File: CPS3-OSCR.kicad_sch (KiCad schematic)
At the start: 17 parts, among them J1 128MB, J2 64MB, J3 CART SLOT TOP ROW, J4 CART SLOT BOTTOM ROW, J5 5145154-1, J6 Conn_02x03_Counter_Clockwise, J7 Conn_02x03_Counter_Clockwise, U1 74LS245, U2 74LS245, U3 74LS245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

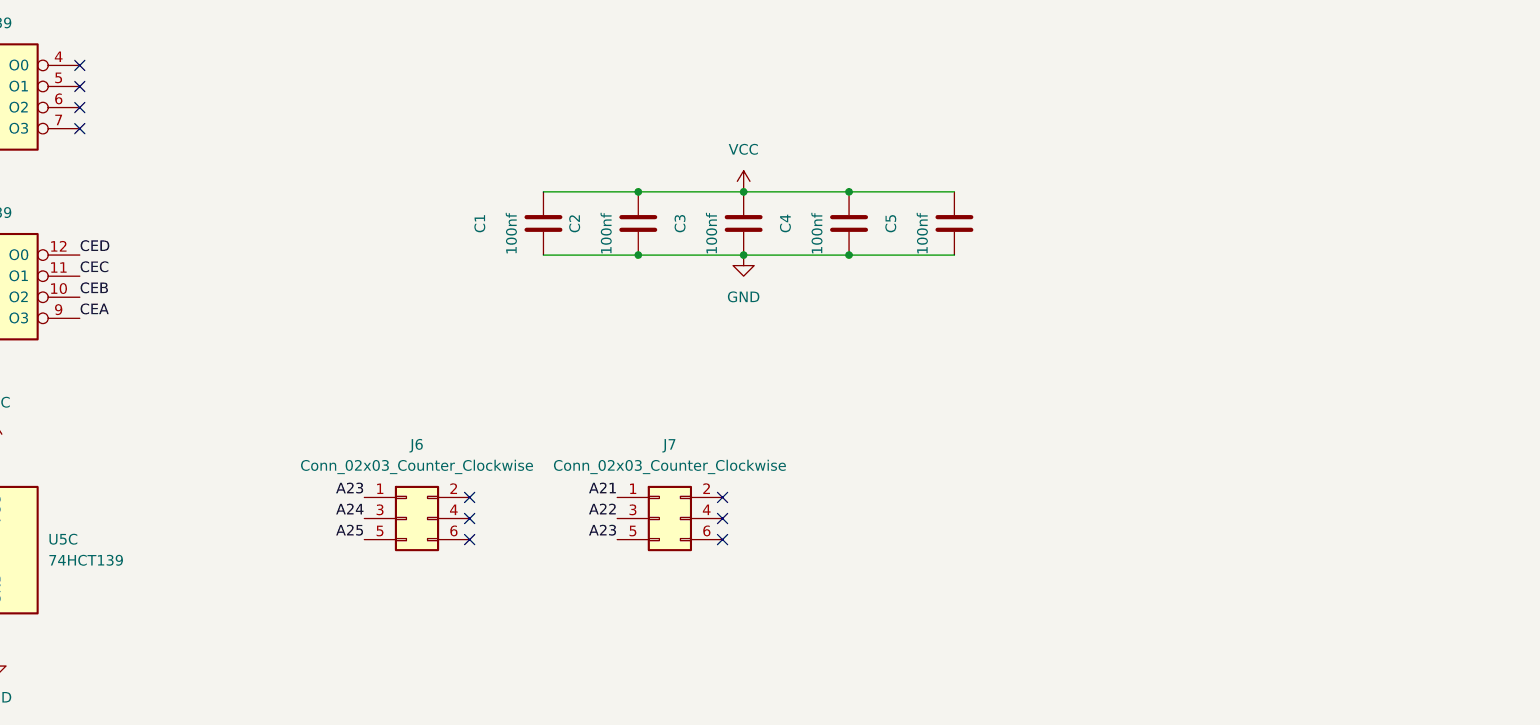
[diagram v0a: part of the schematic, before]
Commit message: Add voltage divider resitor to 3.3V and pullup's disable ic's as default
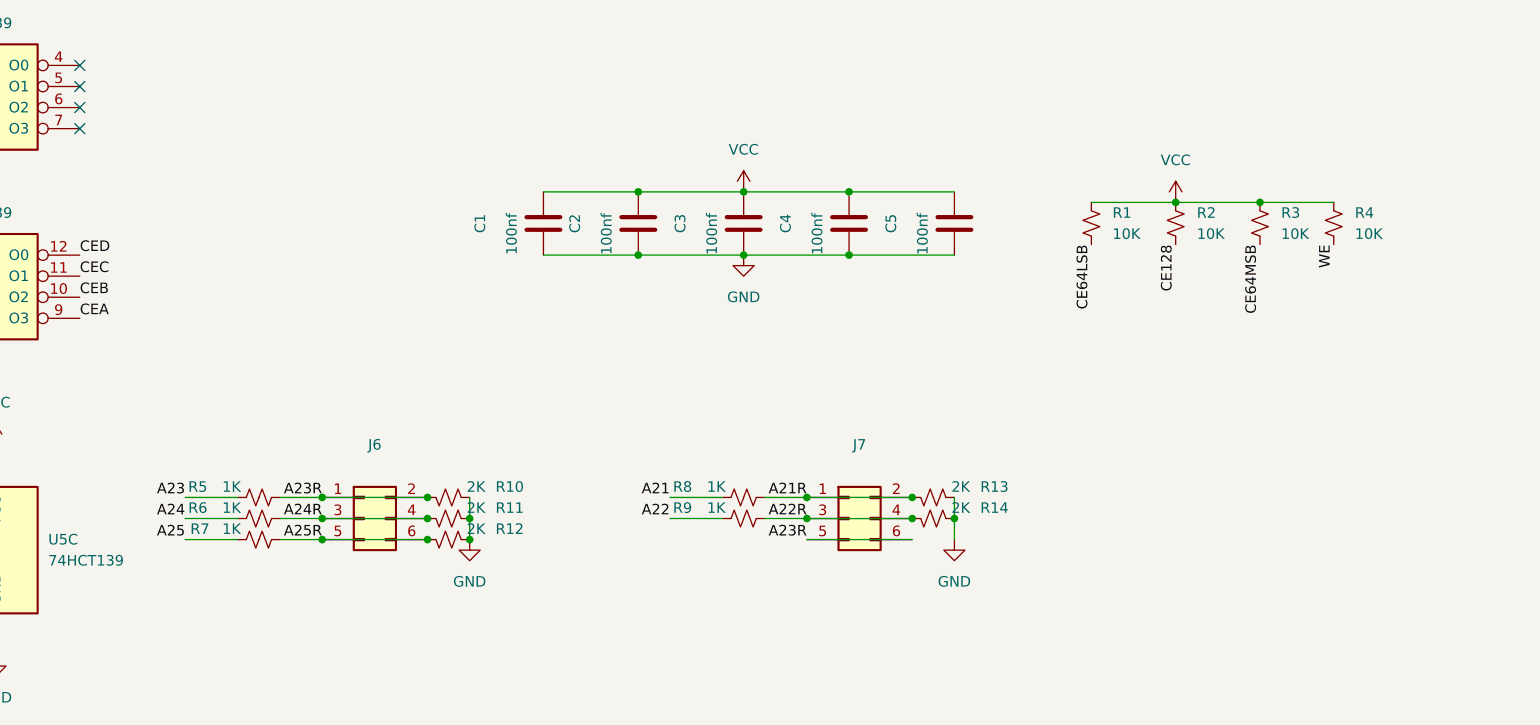
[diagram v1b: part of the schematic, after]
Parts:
- added R1, R2, R3, R4: 10K, Resistor_SMD:R_0805_2012Metric, symbol Device:R_Small_US
- added R10, R11, R12, R13, R14: 2K, Resistor_SMD:R_0805_2012Metric, symbol Device:R_Small_US
- added R5, R6, R7, R8, R9: 1K, Resistor_SMD:R_0805_2012Metric, symbol Device:R_Small_US
- U1, U2, U3, U4: footprint Package_SO:SSOP-20_5.3x7.2mm_P0.65mm -> CPS3:SSOP-20_5.3x7.2mm_P0.65mm_.45
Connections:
- net A21: now also R8.1; no longer J7.1 (Pin_1)
- net A22: now also R9.1; no longer J7.3 (Pin_3)
- net A23: now also R5.1; no longer J6.1 (Pin_1), J7.5 (Pin_5)
- net A24: now also R6.1; no longer J6.3 (Pin_3)
- net A25: now also R7.1; no longer J6.5 (Pin_5)
- net CE128: now also R2.2
- net CE64LSB: now also R1.2
- net CE64MSB: now also R3.2
- net GND: now also R10.1, R11.1, R12.1, R13.1, R14.1
- net VCC: now also R1.1, R2.1, R3.1, R4.1
- net WE: now also R4.2
- net A21R: now reaches J7.2 (Pin_2)
- net A21R: now also J7.1 (Pin_1), R13.2, R8.2
- net A22R: now reaches J7.4 (Pin_4)
- net A22R: now also J7.3 (Pin_3), R14.2, R9.2
- net A23R: now reaches J7.6 (Pin_6)
- net A23R: now also J6.1 (Pin_1), J6.2 (Pin_2), J7.5 (Pin_5), R10.2, R5.2
- net A24R: now reaches J6.4 (Pin_4)
- net A24R: now also J6.3 (Pin_3), R11.2, R6.2
- net A25R: now reaches J6.6 (Pin_6)
- net A25R: now also J6.5 (Pin_5), R12.2, R7.2
- no-connect marks 60 -> 54
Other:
- moved on the sheet: J6, J7
